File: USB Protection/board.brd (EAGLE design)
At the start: 25.4 x 17.8 mm, 5 parts, among them J1 USB-MB-H

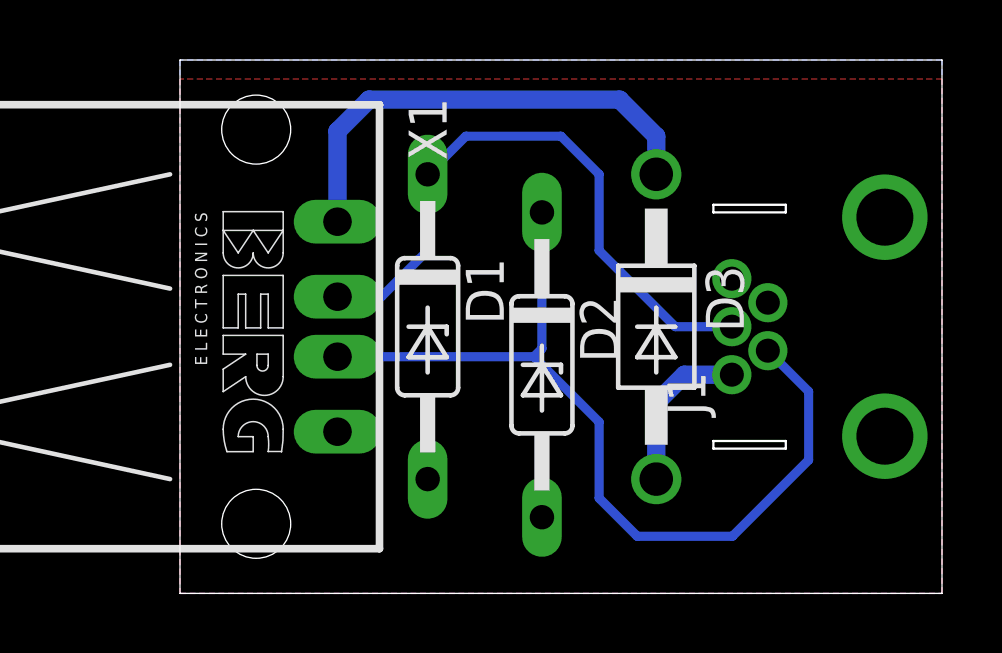
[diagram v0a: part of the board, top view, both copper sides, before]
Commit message: Nano++ schematic; guitar hero redo to not use 1/64th bit
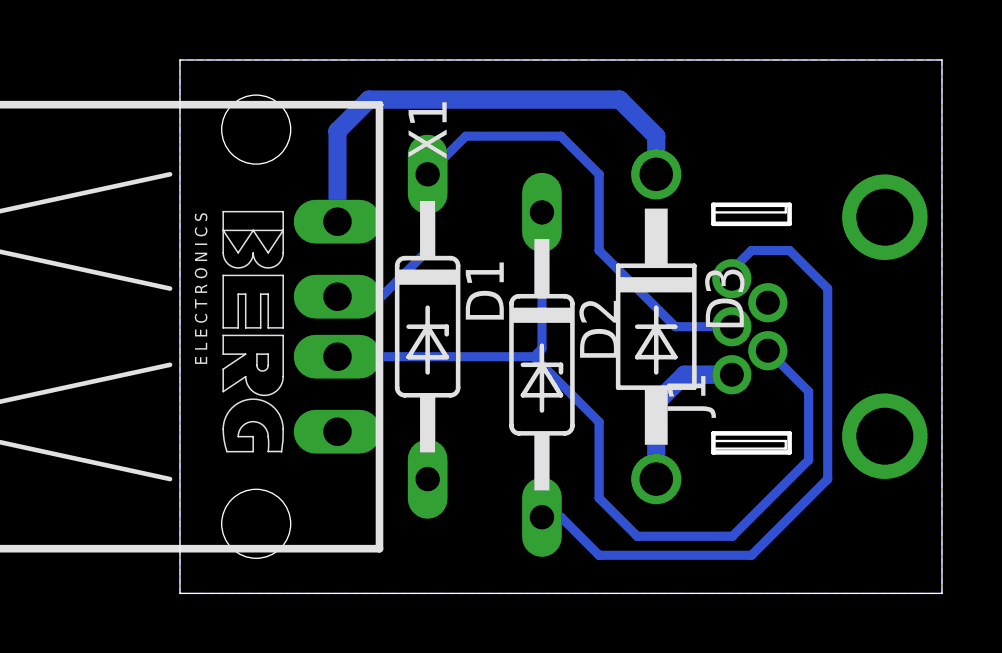
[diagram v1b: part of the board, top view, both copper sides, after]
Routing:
- net GND: track 0.00 -> 21.7 mm
- removed copper zone on layer 1, net GND
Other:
- outline, holes or cut-outs redrawn
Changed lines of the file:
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@@
 <setting verticaltext="up"/>
 </settings>
-<grid distance="25" unitdist="mil" unit="mil" style="lines" multiple="1" display="yes" altdistance="5" altunitdist="mil" altunit="mil"/>
+<grid distance="5" unitdist="mil" unit="mil" style="lines" multiple="1" display="yes" altdistance="5" altunitdist="mil" altunit="mil"/>
 <layers>
 <layer number="1" name="Top" color="4" fill="1" visible="yes" active="yes"/>
@@
 <vertex x="23.495" y="8.636"/>
 <vertex x="25.908" y="8.636"/>
+</polygon>
+<polygon width="0.1524" layer="41">
+<vertex x="22.86" y="9.525"/>
+<vertex x="22.86" y="8.255"/>
+<vertex x="26.67" y="8.255"/>
+<vertex x="26.67" y="9.525"/>
+</polygon>
+<polygon width="0.1524" layer="41">
+<vertex x="26.67" y="17.145"/>
+<vertex x="22.86" y="17.145"/>
+<vertex x="22.86" y="15.875"/>
+<vertex x="26.67" y="15.875"/>
+</polygon>
+<polygon width="0.1524" layer="42">
+<vertex x="22.86" y="17.145"/>
+<vertex x="22.86" y="15.875"/>
+<vertex x="26.67" y="15.875"/>
+<vertex x="26.67" y="17.145"/>
+</polygon>
+<polygon width="0.1524" layer="42">
+<vertex x="22.86" y="9.525"/>
+<vertex x="22.86" y="8.255"/>
+<vertex x="26.67" y="8.255"/>
+<vertex x="26.67" y="9.525"/>
+</polygon>
+<polygon width="0.1524" layer="46">
+<vertex x="23.495" y="16.764"/>
+<vertex x="23.495" y="16.129"/>
+<vertex x="26.035" y="16.129"/>
+<vertex x="26.035" y="16.764"/>
+</polygon>
+<polygon width="0.1524" layer="46">
+<vertex x="23.495" y="8.509"/>
+<vertex x="23.495" y="9.144"/>
+<vertex x="26.035" y="9.144"/>
+<vertex x="26.035" y="8.509"/>
 </polygon>
 </plain>
@@
 <contactref element="D1" pad="A"/>
 <contactref element="D2" pad="A"/>
-<polygon width="0.3048" layer="16" isolate="0.3048">
+<polygon width="0.3048" layer="16" isolate="0.635">
 <vertex x="5.715" y="21.59"/>
 <vertex x="5.715" y="3.81"/>
@@
 <vertex x="31.115" y="21.59"/>
 </polygon>
-<polygon width="0.3048" layer="1" isolate="0.3048">
-<vertex x="5.715" y="20.955"/>
-<vertex x="5.715" y="3.81"/>
-<vertex x="31.115" y="3.81"/>
-<vertex x="31.115" y="20.955"/>
-</polygon>
+<wire x1="24.11" y1="14.3" x2="24.11" y2="14.585" width="0.3048" layer="16"/>
+<wire x1="24.11" y1="14.585" x2="24.765" y2="15.24" width="0.3048" layer="16"/>
+<wire x1="24.765" y1="15.24" x2="26.035" y2="15.24" width="0.3048" layer="16"/>
+<wire x1="26.035" y1="15.24" x2="27.305" y2="13.97" width="0.3048" layer="16"/>
+<wire x1="27.305" y1="13.97" x2="27.305" y2="7.62" width="0.3048" layer="16"/>
+<wire x1="27.305" y1="7.62" x2="24.765" y2="5.08" width="0.3048" layer="16"/>
+<wire x1="19.685" y1="5.08" x2="18.415" y2="6.35" width="0.3048" layer="16"/>
+<wire x1="18.415" y1="6.35" x2="17.78" y2="6.35" width="0.3048" layer="16"/>
+<wire x1="24.765" y1="5.08" x2="19.685" y2="5.08" width="0.3048" layer="16"/>
 </signal>
 <signal name="VBUS">

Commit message: Added lab 6
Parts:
- removed D1, D2: 1N821, diode:DO35Z10
- removed X1: (no value), con-berg:PN87520
- added ENABLE: (no value), pinhead:1X02
- added IC1: LM741P, linear:DIL08
- added Q1: (no value), transistor-power:TO220BV
- added R1: 560, resistor:0207/7
- added R2, R3: (no value), resistor:0207/7
- added USB_A: (no value), con-usb-3:USB-A-H
- D3: value 1N4942 -> BZX55Z2V0; device diode:DO41-10 -> diode:DO35-7
- moved J1 28.5 mm to (55.9, 22.9)
- moved D3 21.7 mm to (41.9, 20.3), turned to 0 degrees
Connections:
- removed net N$1: D3.C, X1.1
- new net VBUS_IN: ENABLE.1, J1.VBUS
- new net VREF: D3.C, IC1.2, R1.1
- new net V_EDIV: IC1.3, R2.1, R3.2
- new net V_EN: IC1.6, Q1.G
- new net V_EXT: Q1.S, R2.2, USB_A.VBUS
- net D+: now also USB_A.D+; no longer D2.C, X1.3
- net D-: now also USB_A.D-; no longer D1.C, X1.2
- net GND: now also D3.A, IC1.4, R3.1, USB_A.GND; no longer D1.A, D2.A, X1.4
- net VBUS: now also ENABLE.2, IC1.7, Q1.D, R1.2; no longer D3.A, J1.VBUS
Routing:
- net GND: track 21.7 -> 0.00 mm
- net V_EXT: track 0.00 -> 21.4 mm
- net VBUS: track 5.45 -> 26.0 mm
- net V_EDIV: track 0.00 -> 17.3 mm
- net VREF: track 0.00 -> 17.0 mm
- net N$1: track 15.9 -> 0.00 mm
- net V_EN: track 0.00 -> 14.3 mm
- net D-: track 21.0 -> 34.9 mm
- net VBUS_IN: track 0.00 -> 10.2 mm
- net D+: track 29.9 -> 39.9 mm
- added copper zone on layer 1, net GND
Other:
- board size 25.4 x 17.8 mm -> 43.2 x 17.8 mm
- board text added: "TH"
